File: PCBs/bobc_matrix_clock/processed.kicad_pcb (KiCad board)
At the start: 2 copper layers, 100 x 98 mm, 36 parts, among them P1 IN, P2 OUT, U1 MAX7219, U2 MAX7219, U3 MAX7219, U4 MAX7219, U5 MAX7219

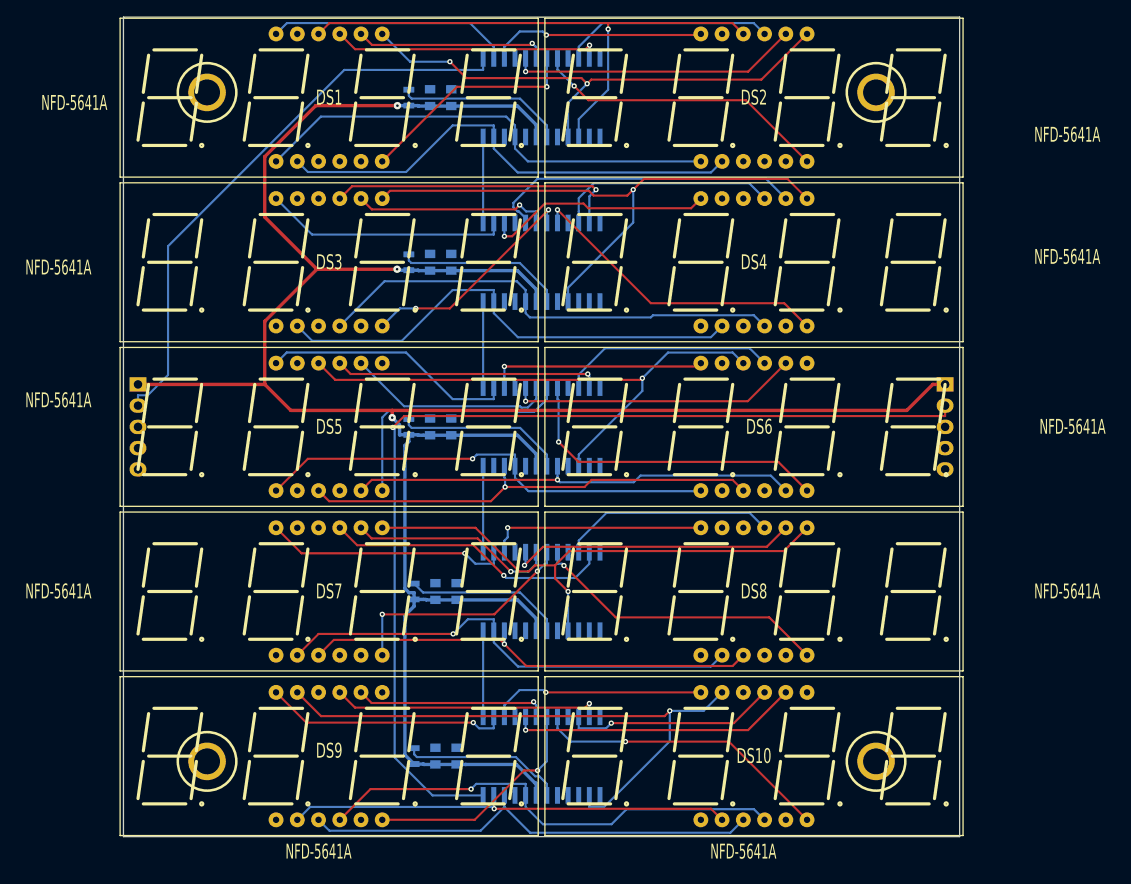
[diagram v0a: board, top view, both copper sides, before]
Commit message: recheck all circuits and clean up fill zone by rerouting the nets using freerouting and manually
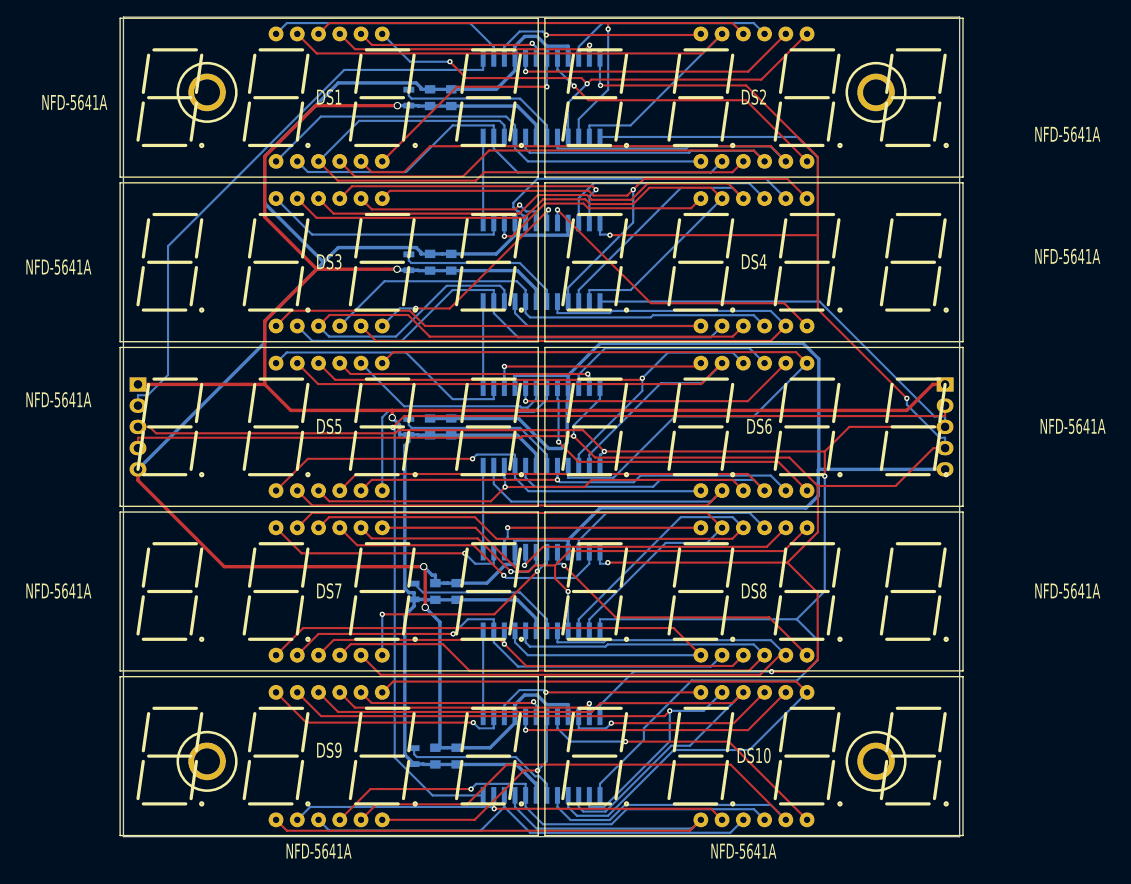
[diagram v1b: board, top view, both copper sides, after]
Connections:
- C1 pad 2: (no net) -> GND
- C10 pad 2: (no net) -> GND
- C2 pad 2: (no net) -> GND
- C3 pad 2: (no net) -> GND
- C4 pad 2: (no net) -> GND
- C5 pad 2: (no net) -> GND
- C6 pad 2: (no net) -> GND
- C7 pad 2: (no net) -> GND
- C8 pad 2: (no net) -> GND
- C9 pad 2: (no net) -> GND
- DS1 pad 11: (no net) -> /Digits Row 1/SEG_A
- DS1 pad 3: (no net) -> /Digits Row 1/SEG_DP
- DS1 pad 4: (no net) -> /Digits Row 1/SEG_C
- DS1 pad 5: (no net) -> /Digits Row 1/SEG_G
- DS10 pad 1: (no net) -> /Row 5/SEG_E
- DS10 pad 10: (no net) -> /Row 5/SEG_F
- DS10 pad 5: (no net) -> /Row 5/SEG_G
- DS10 pad 7: (no net) -> /Row 5/SEG_B
- DS2 pad 11: (no net) -> /Digits Row 1/SEG_A
- DS2 pad 3: (no net) -> /Digits Row 1/SEG_DP
- DS2 pad 4: (no net) -> /Digits Row 1/SEG_C
- DS2 pad 5: (no net) -> /Digits Row 1/SEG_G
- DS3 pad 1: (no net) -> /Row 2/SEG_E
- DS3 pad 10: (no net) -> /Row 2/SEG_F
- DS3 pad 11: (no net) -> /Row 2/SEG_A
- DS3 pad 3: (no net) -> /Row 2/SEG_DP
- DS3 pad 5: (no net) -> /Row 2/SEG_G
- DS4 pad 1: (no net) -> /Row 2/SEG_E
- DS4 pad 10: (no net) -> /Row 2/SEG_F
- DS4 pad 11: (no net) -> /Row 2/SEG_A
- DS4 pad 3: (no net) -> /Row 2/SEG_DP
- DS4 pad 5: (no net) -> /Row 2/SEG_G
- DS5 pad 11: (no net) -> /Row 3/SEG_A
- DS5 pad 2: (no net) -> /Row 3/SEG_D
- DS5 pad 4: (no net) -> /Row 3/SEG_C
- DS5 pad 7: (no net) -> /Row 3/SEG_B
- DS6 pad 11: (no net) -> /Row 3/SEG_A
- DS6 pad 2: (no net) -> /Row 3/SEG_D
- DS6 pad 4: (no net) -> /Row 3/SEG_C
- DS6 pad 7: (no net) -> /Row 3/SEG_B
- DS7 pad 1: (no net) -> /Row 4/SEG_E
- DS7 pad 10: (no net) -> /Row 4/SEG_F
- DS7 pad 11: (no net) -> /Row 4/SEG_A
- DS7 pad 4: (no net) -> /Row 4/SEG_C
- DS7 pad 5: (no net) -> /Row 4/SEG_G
- DS8 pad 1: (no net) -> /Row 4/SEG_E
- DS8 pad 10: (no net) -> /Row 4/SEG_F
- DS8 pad 11: (no net) -> /Row 4/SEG_A
- DS8 pad 4: (no net) -> /Row 4/SEG_C
- DS8 pad 5: (no net) -> /Row 4/SEG_G
- DS9 pad 1: (no net) -> /Row 5/SEG_E
- DS9 pad 10: (no net) -> /Row 5/SEG_F
- DS9 pad 5: (no net) -> /Row 5/SEG_G
- DS9 pad 7: (no net) -> /Row 5/SEG_B
- P1 pad 3: (no net) -> /Digits Row 1/CLK
- P1 pad 4: (no net) -> /Digits Row 1/LOAD
- P1 pad 5: (no net) -> GND
- P2 pad 3: (no net) -> /Digits Row 1/CLK
- P2 pad 4: (no net) -> /Digits Row 1/LOAD
- P2 pad 5: (no net) -> GND
- U1 pad 12: (no net) -> /Digits Row 1/LOAD
- U1 pad 13: (no net) -> /Digits Row 1/CLK
- U1 pad 14: (no net) -> /Digits Row 1/SEG_A
- U1 pad 17: (no net) -> /Digits Row 1/SEG_G
- U1 pad 20: (no net) -> /Digits Row 1/SEG_C
- U1 pad 22: (no net) -> /Digits Row 1/SEG_DP
- U1 pad 4: (no net) -> GND
- U1 pad 9: (no net) -> GND
- U2 pad 12: (no net) -> /Digits Row 1/LOAD
- U2 pad 13: (no net) -> /Digits Row 1/CLK
- U2 pad 14: (no net) -> /Row 2/SEG_A
- U2 pad 15: (no net) -> /Row 2/SEG_F
- U2 pad 17: (no net) -> /Row 2/SEG_G
- U2 pad 21: (no net) -> /Row 2/SEG_E
- U2 pad 22: (no net) -> /Row 2/SEG_DP
- U2 pad 4: (no net) -> GND
- U2 pad 9: (no net) -> GND
- U3 pad 12: (no net) -> /Digits Row 1/LOAD
- U3 pad 13: (no net) -> /Digits Row 1/CLK
- U3 pad 14: (no net) -> /Row 3/SEG_A
- U3 pad 16: (no net) -> /Row 3/SEG_B
- U3 pad 20: (no net) -> /Row 3/SEG_C
- U3 pad 23: (no net) -> /Row 3/SEG_D
- U3 pad 4: (no net) -> GND
- U3 pad 9: (no net) -> GND
- U4 pad 12: (no net) -> /Digits Row 1/LOAD
- U4 pad 13: (no net) -> /Digits Row 1/CLK
- U4 pad 14: (no net) -> /Row 4/SEG_A
- U4 pad 15: (no net) -> /Row 4/SEG_F
- U4 pad 17: (no net) -> /Row 4/SEG_G
- U4 pad 20: (no net) -> /Row 4/SEG_C
- U4 pad 21: (no net) -> /Row 4/SEG_E
- U4 pad 4: (no net) -> GND
- U4 pad 9: (no net) -> GND
- U5 pad 12: (no net) -> /Digits Row 1/LOAD
- U5 pad 13: (no net) -> /Digits Row 1/CLK
- U5 pad 15: (no net) -> /Row 5/SEG_F
- U5 pad 16: (no net) -> /Row 5/SEG_B
- U5 pad 17: (no net) -> /Row 5/SEG_G
- U5 pad 21: (no net) -> /Row 5/SEG_E
- U5 pad 4: (no net) -> GND
- U5 pad 9: (no net) -> GND
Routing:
- net GND: track 0.00 -> 368.3 mm, vias 0 -> 2
- net /Digits Row 1/LOAD: track 0.00 -> 288.4 mm, vias 0 -> 6
- net /Digits Row 1/CLK: track 0.00 -> 280.5 mm, vias 0 -> 2
- net /Row 5/SEG_B: track 0.00 -> 88.4 mm
- net /Row 3/SEG_B: track 0.00 -> 87.5 mm
- net /Row 5/SEG_G: track 0.00 -> 87.1 mm
- net /Row 4/SEG_C: track 0.00 -> 84.2 mm
- net /Digits Row 1/SEG_C: track 0.00 -> 84.2 mm
- net /Row 3/SEG_C: track 0.00 -> 83.7 mm
- net /Row 3/SEG_D: track 0.00 -> 83.1 mm
- net /Digits Row 1/SEG_G: track 0.00 -> 82.9 mm
- net /Row 4/SEG_G: track 0.00 -> 82.3 mm
- net /Row 2/SEG_G: track 0.00 -> 81.8 mm
- net /Row 2/SEG_F: track 0.00 -> 80.9 mm
- net /Row 5/SEG_F: track 0.00 -> 79.9 mm
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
